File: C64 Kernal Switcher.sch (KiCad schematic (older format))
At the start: 9 parts, among them IC1 ArduinoProMini, J1 LED, J2 Signals, U1 2364, U2 28C256

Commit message: Fixed footprints
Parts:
- IC1: footprint mysensors_arduino:pro_mini_china -> mysensors_arduino:pro_mini
- J1, J2, JP1, JP2: footprint (none) -> Pin_Headers:Pin_Header_Straight_1x03_Pitch2.54mm
- R1, R2: footprint (none) -> Resistors_THT:R_Axial_DIN0207_L6.3mm_D2.5mm_P10.16mm_Horizontal
- U1: footprint (none) -> Housings_DIP:DIP-24_W15.24mm_Socket
- U2: footprint (none) -> Housings_DIP:DIP-28_W15.24mm_Socket
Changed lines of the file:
@@
 F 0 "U2" H 5325 3775 50  0000 C CNN
 F 1 "28C256" H 5425 1775 50  0000 C CNN
-F 2 "" H 5125 2775 50  0001 C CNN
+F 2 "Housings_DIP:DIP-28_W15.24mm_Socket" H 5125 2775 50  0001 C CNN
 F 3 "" H 5125 2775 50  0001 C CNN
 	1    5125 2775
@@
 F 0 "U1" H 2900 3775 50  0000 C CNN
 F 1 "2364" H 3000 1775 50  0000 C CNN
-F 2 "" H 2700 2775 50  0001 C CNN
+F 2 "Housings_DIP:DIP-24_W15.24mm_Socket" H 2700 2775 50  0001 C CNN
 F 3 "" H 2700 2775 50  0001 C CNN
 	1    2700 2775
@@
 F 0 "JP1" H 6925 1525 50  0000 L CNN
 F 1 "A13_SEL" H 6875 1725 50  0000 C BNN
-F 2 "" H 6875 1625 50  0001 C CNN
+F 2 "Pin_Headers:Pin_Header_Straight_1x03_Pitch2.54mm" H 6875 1625 50  0001 C CNN
 F 3 "" H 6875 1625 50  0001 C CNN
 	1    6875 1625
@@
 F 0 "JP2" H 7200 2100 50  0000 L CNN
 F 1 "A14_SEL" H 7150 2300 50  0000 C BNN
-F 2 "" H 7150 2200 50  0001 C CNN
+F 2 "Pin_Headers:Pin_Header_Straight_1x03_Pitch2.54mm" H 7150 2200 50  0001 C CNN
 F 3 "" H 7150 2200 50  0001 C CNN
 	1    7150 2200
@@
 F 0 "IC1" H 1950 7425 40  0000 L BNN
 F 1 "ArduinoProMini" H 3100 4775 40  0000 L BNN
-F 2 "mysensors_arduino:pro_mini_china" H 2700 6175 30  0001 C CIN
+F 2 "mysensors_arduino:pro_mini" H 2700 6175 30  0001 C CIN
 F 3 "" H 2700 6175 60  0000 C CNN
 	1    2700 6175
@@
 F 0 "J1" H 6675 5050 50  0000 C CNN
 F 1 "LED" H 6675 4650 50  0000 C CNN
-F 2 "" H 6675 4850 50  0001 C CNN
+F 2 "Pin_Headers:Pin_Header_Straight_1x03_Pitch2.54mm" H 6675 4850 50  0001 C CNN
 F 3 "" H 6675 4850 50  0001 C CNN
 	1    6675 4850
@@
 F 0 "R1" V 6205 4750 50  0000 C CNN
 F 1 "330" V 6125 4750 50  0000 C CNN
-F 2 "" V 6055 4750 50  0001 C CNN
+F 2 "Resistors_THT:R_Axial_DIN0207_L6.3mm_D2.5mm_P10.16mm_Horizontal" V 6055 4750 50  0001 C CNN
 F 3 "" H 6125 4750 50  0001 C CNN
 	1    6125 4750
@@
 F 0 "R2" V 6205 4950 50  0000 C CNN
 F 1 "330" V 6125 4950 50  0000 C CNN
-F 2 "" V 6055 4950 50  0001 C CNN
+F 2 "Resistors_THT:R_Axial_DIN0207_L6.3mm_D2.5mm_P10.16mm_Horizontal" V 6055 4950 50  0001 C CNN
 F 3 "" H 6125 4950 50  0001 C CNN
 	1    6125 4950
@@
 F 0 "J2" H 6675 5975 50  0000 C CNN
 F 1 "Signals" H 6675 5575 50  0000 C CNN
-F 2 "" H 6675 5775 50  0001 C CNN
+F 2 "Pin_Headers:Pin_Header_Straight_1x03_Pitch2.54mm" H 6675 5775 50  0001 C CNN
 F 3 "" H 6675 5775 50  0001 C CNN
 	1    6675 5775

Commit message: PCB layed out, need measuring
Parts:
- removed IC1: ArduinoProMini, mysensors_arduino:pro_mini, symbol ArduinoProMini
- added A1: Arduino_Nano_v3.x, Modules:Arduino_Nano, symbol Arduino_Nano_v3.x
- added J3: Power, Pin_Headers:Pin_Header_Straight_1x02_Pitch2.54mm, symbol Conn_01x02
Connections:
- net labels added: LED1, LED2
- net labels removed: LED, LED_ALT
- wire segments 75 -> 76
- no-connect marks 18 -> 20
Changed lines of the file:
@@
 LIBS:valves
 LIBS:2364
-LIBS:mysensors_arduino
+LIBS:modules
 LIBS:C64 Kernal Switcher-cache
 EELAYER 25 0
@@
 	6175 2100 6275 2200
 $Comp
-L ArduinoProMini IC1
-U 1 1 5CC73261
-P 2700 6175
-F 0 "IC1" H 1950 7425 40  0000 L BNN
-F 1 "ArduinoProMini" H 3100 4775 40  0000 L BNN
-F 2 "mysensors_arduino:pro_mini" H 2700 6175 30  0001 C CIN
-F 3 "" H 2700 6175 60  0000 C CNN
-	1    2700 6175
-	1    0    0    -1
-$EndComp
-$Comp
 L VCC #PWR08
 U 1 1 5CC73368
-P 1725 5000
-F 0 "#PWR08" H 1725 4850 50  0001 C CNN
-F 1 "VCC" H 1725 5150 50  0000 C CNN
-F 2 "" H 1725 5000 50  0001 C CNN
-F 3 "" H 1725 5000 50  0001 C CNN
-	1    1725 5000
+P 3625 4850
+F 0 "#PWR08" H 3625 4700 50  0001 C CNN
+F 1 "VCC" H 3625 5000 50  0000 C CNN
+F 2 "" H 3625 4850 50  0001 C CNN
+F 3 "" H 3625 4850 50  0001 C CNN
+	1    3625 4850
 	1    0    0    -1
 $EndComp
@@
 L GND #PWR09
 U 1 1 5CC734A8
-P 1725 7450
-F 0 "#PWR09" H 1725 7200 50  0001 C CNN
-F 1 "GND" H 1725 7300 50  0000 C CNN
-F 2 "" H 1725 7450 50  0001 C CNN
-F 3 "" H 1725 7450 50  0001 C CNN
-	1    1725 7450
-	1    0    0    -1
-$EndComp
-Text GLabel 3775 5475 2    60   Output ~ 0
-LED
-Text GLabel 3775 6275 2    60   Output ~ 0
-LED_ALT
-Text GLabel 3775 5575 2    60   Output ~ 0
+P 2850 7075
+F 0 "#PWR09" H 2850 6825 50  0001 C CNN
+F 1 "GND" H 2850 6925 50  0000 C CNN
+F 2 "" H 2850 7075 50  0001 C CNN
+F 3 "" H 2850 7075 50  0001 C CNN
+	1    2850 7075
+	1    0    0    -1
+$EndComp
+Text GLabel 2175 5725 0    60   Output ~ 0
+LED1
+Text GLabel 2175 5825 0    60   Output ~ 0
 A13
-Text GLabel 3775 5675 2    60   Output ~ 0
+Text GLabel 2175 5925 0    60   Output ~ 0
 A14
-Text GLabel 3775 5775 2    60   BiDi ~ 0
+Text GLabel 2175 6025 0    60   BiDi ~ 0
 RESET
-Text GLabel 3775 5875 2    60   Input ~ 0
+Text GLabel 2175 5625 0    60   Input ~ 0
 ESXROM
-Text GLabel 3775 5975 2    60   Input ~ 0
+Text GLabel 2175 6125 0    60   Input ~ 0
 RESTORE
-NoConn ~ 1800 5375
-NoConn ~ 1800 6875
-NoConn ~ 1800 6975
-NoConn ~ 3700 6075
-NoConn ~ 3700 6375
-NoConn ~ 3700 6475
-NoConn ~ 3700 6675
-NoConn ~ 3700 6775
-NoConn ~ 3700 6875
-NoConn ~ 3700 6975
-NoConn ~ 3700 7075
-NoConn ~ 3700 7175
-NoConn ~ 3700 7275
-NoConn ~ 3700 7375
-NoConn ~ 3700 5075
-NoConn ~ 3700 5175
-NoConn ~ 3700 5275
-NoConn ~ 3700 5375
+NoConn ~ 2850 4925
+NoConn ~ 2250 6425
+NoConn ~ 2250 6325
+NoConn ~ 3250 5925
+NoConn ~ 3250 6025
+NoConn ~ 3250 6125
+NoConn ~ 3250 6225
+NoConn ~ 3250 6325
+NoConn ~ 3250 6425
+NoConn ~ 3250 6525
+NoConn ~ 3250 6625
 $Comp
 L Conn_01x03 J1
@@
 $EndComp
 Text GLabel 5900 4750 0    60   Input ~ 0
-LED
+LED1
 Text GLabel 5900 4950 0    60   Input ~ 0
-LED_ALT
+LED2
 $Comp
 L R R1
@@
 Connection ~ 4350 3575
 Wire Wire Line
-	1725 5000 1725 5075
-Wire Wire Line
-	1725 5075 1800 5075
-Wire Wire Line
-	1725 7175 1725 7450
-Wire Wire Line
-	1725 7375 1800 7375
-Wire Wire Line
-	1725 7175 1800 7175
-Connection ~ 1725 7375
-Wire Wire Line
-	1800 7275 1725 7275
-Connection ~ 1725 7275
-Wire Wire Line
-	3700 5475 3775 5475
-Wire Wire Line
-	3700 5575 3775 5575
-Wire Wire Line
-	3700 5675 3775 5675
-Wire Wire Line
-	3700 5775 3775 5775
-Wire Wire Line
-	3700 5875 3775 5875
-Wire Wire Line
-	3700 5975 3775 5975
-Wire Wire Line
-	3700 6275 3775 6275
+	2250 5725 2175 5725
+Wire Wire Line
+	2250 5825 2175 5825
+Wire Wire Line
+	2250 5925 2175 5925
+Wire Wire Line
+	2250 6025 2175 6025
+Wire Wire Line
+	2250 5625 2175 5625
+Wire Wire Line
+	2250 6125 2175 6125
 Wire Wire Line
 	5900 4750 5975 4750
@@
 	1    0    0    -1
 $EndComp
-Text GLabel 6400 5675 0    60   BiDi ~ 0
+Text GLabel 6400 5775 0    60   BiDi ~ 0
 RESET
 Wire Wire Line
 	6400 5675 6475 5675
-Text GLabel 6400 5775 0    60   Output ~ 0
+Text GLabel 6400 5675 0    60   Output ~ 0
 ESXROM
 Text GLabel 6400 5875 0    60   Output ~ 0
@@
 Wire Wire Line
 	6400 5875 6475 5875
+$Comp
+L Arduino_Nano_v3.x A1
+U 1 1 5CC769CE
+P 2750 5925
+F 0 "A1" H 2550 6950 50  0000 R CNN
+F 1 "Arduino_Nano_v3.x" H 2550 6875 50  0000 R CNN
+F 2 "Modules:Arduino_Nano" H 2900 4975 50  0001 L CNN
+F 3 "" H 2750 4925 50  0001 C CNN
+	1    2750 5925
+	1    0    0    -1
+$EndComp
+NoConn ~ 2650 4925
+NoConn ~ 3250 5725
+NoConn ~ 3250 5325
+NoConn ~ 3250 5425
+NoConn ~ 2250 5325
+NoConn ~ 2250 5425
+NoConn ~ 2250 5525
+Text GLabel 2175 6225 0    60   Output ~ 0
+LED2
+Wire Wire Line
+	2250 6225 2175 6225
+NoConn ~ 2250 6525
+Wire Wire Line
+	2750 6925 2750 7000
+Wire Wire Line
+	2750 7000 2850 7000
+Wire Wire Line
+	2850 6925 2850 7075
+Connection ~ 2850 7000
+NoConn ~ 2250 6625
+$Comp
+L Conn_01x02 J3
+U 1 1 5CC7857E
+P 3625 5125
+F 0 "J3" H 3625 5225 50  0000 C CNN
+F 1 "Power" H 3625 4925 50  0000 C CNN
+F 2 "Pin_Headers:Pin_Header_Straight_1x02_Pitch2.54mm" H 3625 5125 50  0001 C CNN
+F 3 "" H 3625 5125 50  0001 C CNN
+	1    3625 5125
+	0    1    1    0
+$EndComp
+Wire Wire Line
+	3625 4850 3625 4925
+Wire Wire Line
+	3525 4925 3525 4850
+Wire Wire Line
+	3525 4850 2950 4850
+Wire Wire Line
+	2950 4850 2950 4925
 $EndSCHEMATC

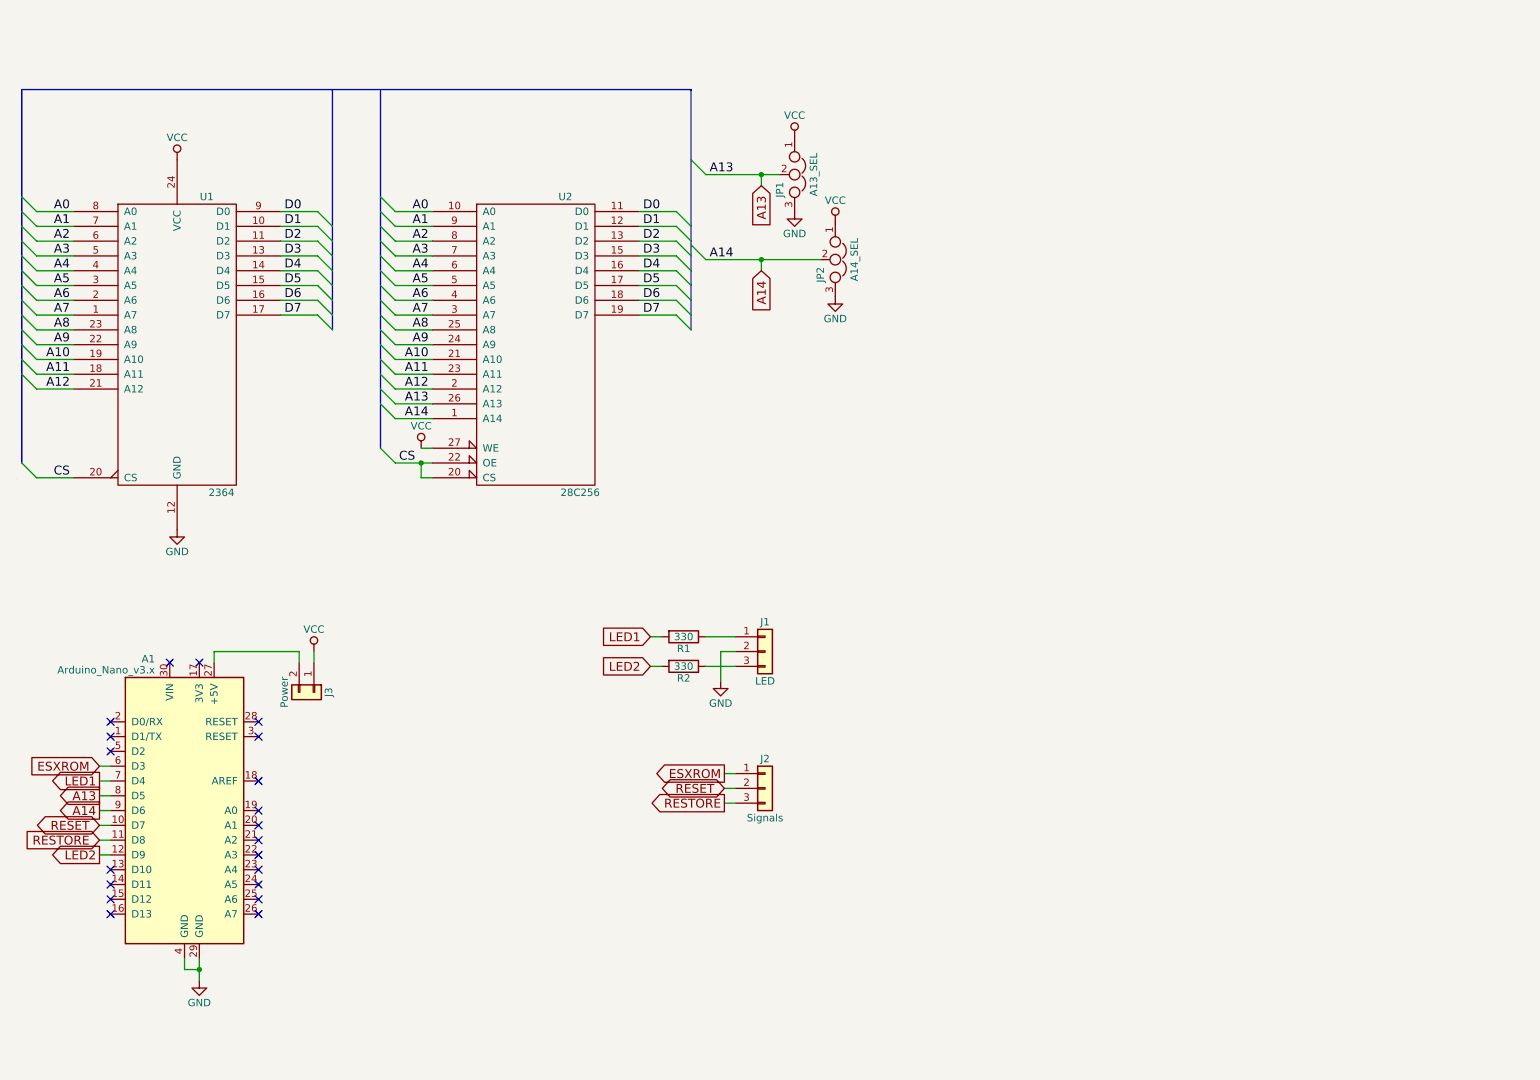
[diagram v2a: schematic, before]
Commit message: Changed to PIC like bwack's design
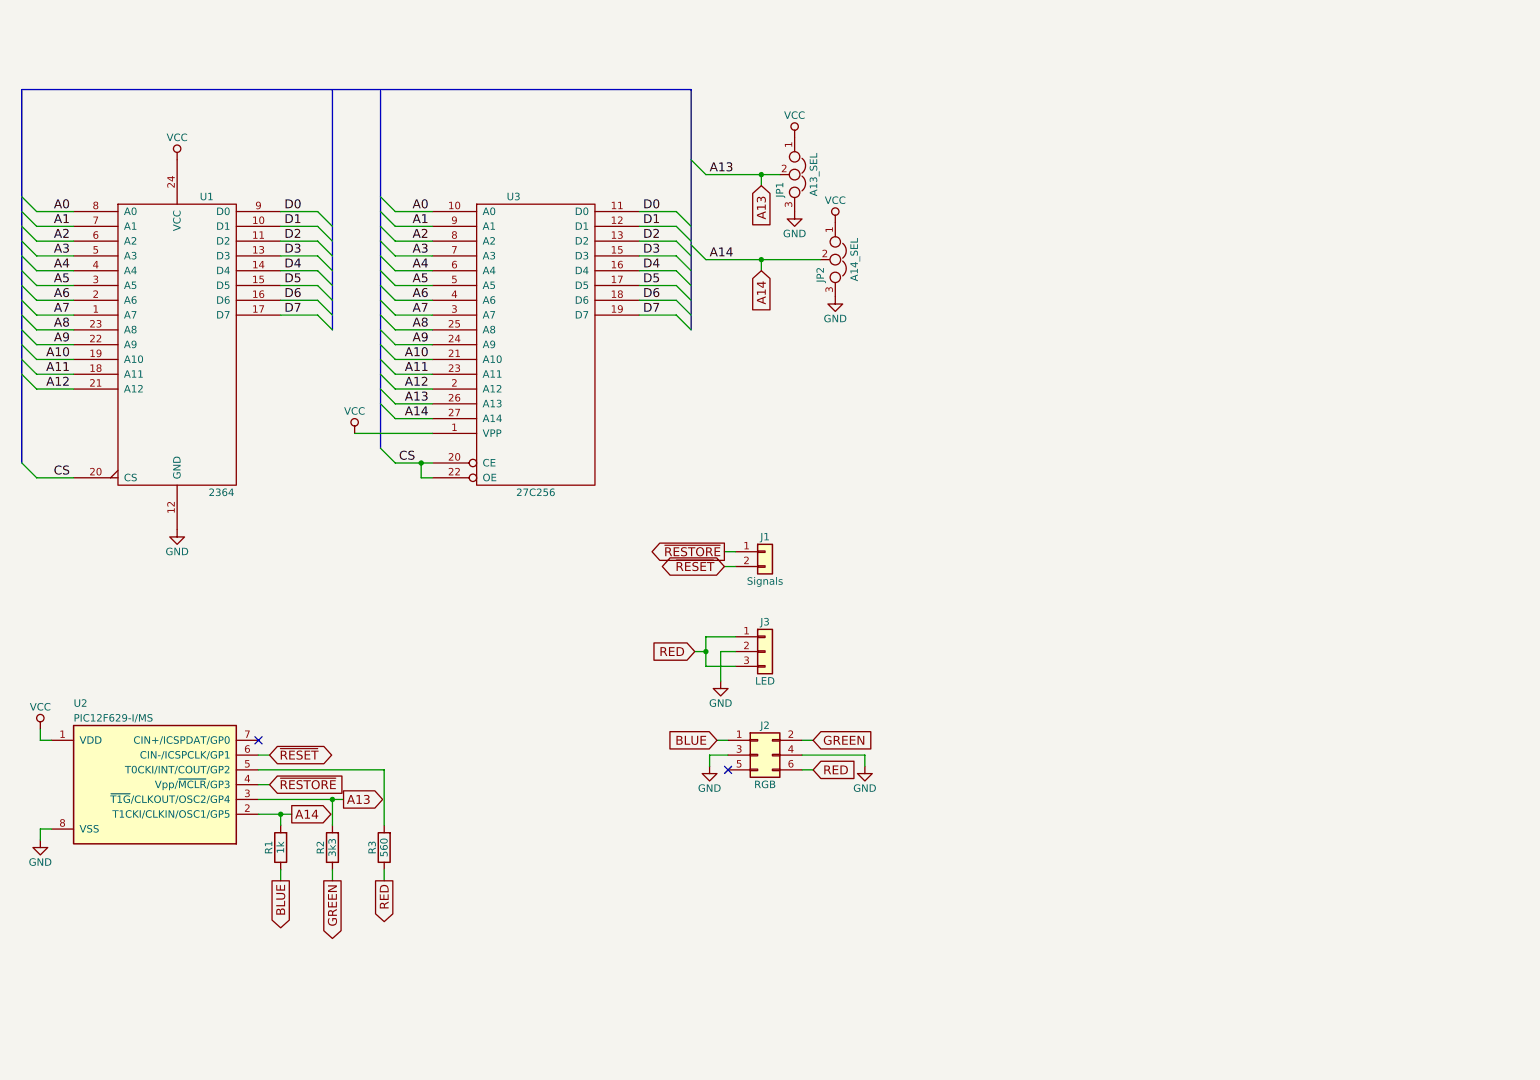
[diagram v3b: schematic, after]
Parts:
- removed A1: Arduino_Nano_v3.x, Modules:Arduino_Nano, symbol Arduino_Nano_v3.x
- removed J2: Signals, Pin_Headers:Pin_Header_Straight_1x03_Pitch2.54mm, symbol Conn_01x03
- removed J3: Power, Pin_Headers:Pin_Header_Straight_1x02_Pitch2.54mm, symbol Conn_01x02
- removed U2: 28C256, Housings_DIP:DIP-28_W15.24mm_Socket, symbol 28C256
- added J1: Signals, symbol Conn_01x02
- added J2: RGB, symbol Conn_02x03_Odd_Even
- added R3: 560, Resistors_THT:R_Axial_DIN0207_L6.3mm_D2.5mm_P10.16mm_Horizontal, symbol R
- added U2: PIC12F629-I/MS, symbol PIC12F629-I/MS
- added U3: 27C256, symbol 27C256
- R1: value 330 -> 1k
- R2: value 330 -> 3k3
- renumbered J1 to J3
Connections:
- net LED1 is gone; now on net A14: R1.2
- net LED2 is gone; now on net A13: R2.2
- net A0: now also U3.10 (A0)
- net A1: now also U3.9 (A1)
- net A10: now also U3.21 (A10)
- net A11: now also U3.23 (A11)
- net A12: now also U3.2 (A12)
- net A13: now also U2.3 (~T1G~/CLKOUT/OSC2/GP4), U3.26 (A13)
- net A14: now also U2.2 (T1CKI/CLKIN/OSC1/GP5), U3.27 (A14)
- net A2: now also U3.8 (A2)
- net A3: now also U3.7 (A3)
- net A4: now also U3.6 (A4)
- net A5: now also U3.5 (A5)
- net A6: now also U3.4 (A6)
- net A7: now also U3.3 (A7)
- net A8: now also U3.25 (A8)
- net A9: now also U3.24 (A9)
- net CS: now also U3.20 (CE), U3.22 (OE)
- net D0: now also U3.11 (D0)
- net D1: now also U3.12 (D1)
- net D2: now also U3.13 (D2)
- net D3: now also U3.15 (D3)
- net D4: now also U3.16 (D4)
- net D5: now also U3.17 (D5)
- net D6: now also U3.18 (D6)
- net D7: now also U3.19 (D7)
- net GND: now also J2.3 (Pin_3), J2.4 (Pin_4), U2.8 (VSS), U3.14 (GND)
- net VCC: now also U2.1 (VDD), U3.1 (VPP), U3.28 (VCC)
- net BLUE: now reaches R1.1
- net BLUE: now also J2.1 (Pin_1); no longer J3.1 (Pin_1)
- net GREEN: now reaches R2.1
- net GREEN: now also J2.2 (Pin_2); no longer J3.3 (Pin_3)
- new net: R3.2, U2.5 (T0CKI/INT/COUT/GP2)
- new net RED: J2.6 (Pin_6), J3.1 (Pin_1), J3.3 (Pin_3), R3.1
- new net ~RESET: J1.2 (Pin_2), U2.6 (CIN-/ICSPCLK/GP1)
- new net ~RESTORE: J1.1 (Pin_1), U2.4 (Vpp/~MCLR~/GP3)
- no-connect marks 20 -> 2
